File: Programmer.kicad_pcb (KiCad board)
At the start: 2 copper layers, 17.8 x 38.1 mm, 10 parts, among them J1 USB_B_Micro, J2 Conn_02x05_Odd_Even, SW1 SW_Push, U1 MKL04Z32VLC4, U2 ADP2108AUJ-3.3

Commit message: Rounded corners, added LED
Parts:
- added D1: LED, LED_SMD:LED_0805_2012Metric_Pad1.15x1.40mm_HandSolder, F.Cu at (139.1, 108.6)
- added R3: 500, Resistor_SMD:R_0805_2012Metric_Pad1.15x1.40mm_HandSolder, F.Cu at (139.1, 106.4)
- moved U2 2.16 mm to (135.0, 108.0)
- moved SW1 0.25 mm to (147.2, 101.0)
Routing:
- net +3V3: track 30.1 -> 33.6 mm
- net Net-(D1-Pad1): track 0.00 -> 3.01 mm
- net GND: track 23.7 -> 25.9 mm, vias 6 -> 7
- net Net-(L1-Pad1): track 3.85 -> 2.62 mm
- net /PTA1: track 33.8 -> 34.3 mm
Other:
- outline, holes or cut-outs redrawn

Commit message: Added silkscreen
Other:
- board text added: "RMTS Programmer Rev 1 Andrew Reilley, 2021"
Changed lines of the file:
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@@
   (general
     (thickness 1.6)
-    (drawings 8)
+    (drawings 9)
     (tracks 155)
     (zones 0)
@@
     )
   )
+  (gr_text "RMTS Programmer Rev 1\nAndrew Reilley, 2021" (at 135.89 101.346 90) (layer B.SilkS)
+    (effects (font (size 1.5 1.5) (thickness 0.3)) (justify mirror))
+  )
   (gr_line (start 131.445 117.094) (end 131.445 83.312) (layer Edge.Cuts) (width 0.1))

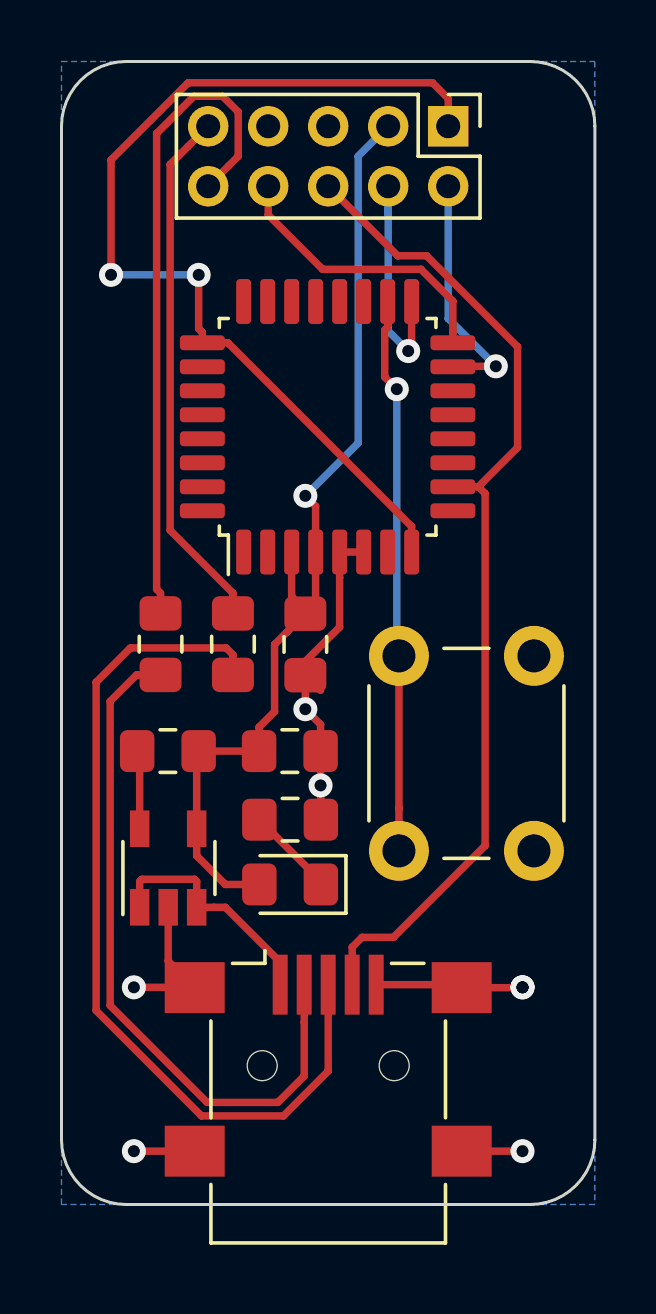
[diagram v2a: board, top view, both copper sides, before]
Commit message: Add input cap
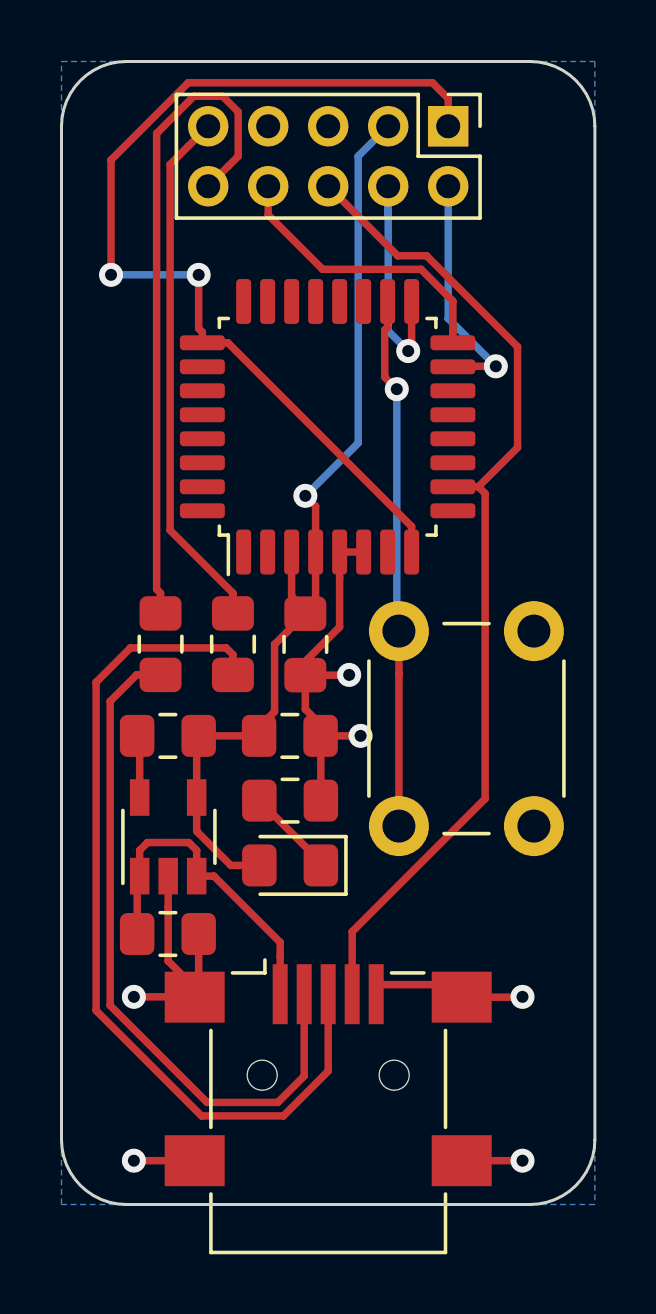
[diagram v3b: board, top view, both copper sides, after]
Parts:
- added C3: 4.7uF, Capacitor_SMD:C_0805_2012Metric_Pad1.15x1.40mm_HandSolder, F.Cu at (135.0, 110.2)
- R1, R2: value R_US -> 33
- moved U2 1.04 mm to (135.0, 107.0)
- moved SW1 0.83 mm to (147.2, 100.1)
- moved R3 0.64 mm to (139.1, 105.8)
- moved D1 0.63 mm to (139.1, 108.0)
- moved C2 0.51 mm to (139.1, 103.6)
- moved L1 0.51 mm to (135.0, 103.6)
- moved J1 0.32 mm to (140.3, 114.9)
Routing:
- net GND: track 25.9 -> 30.2 mm, vias 7 -> 6
- net Net-(C3-Pad1): track 7.97 -> 11.2 mm
- net +3V3: track 33.6 -> 32.8 mm
- net Net-(SW1-Pad2): track 18.8 -> 19.5 mm
- net Net-(L1-Pad1): track 2.62 -> 2.09 mm

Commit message: Provide 5v to target
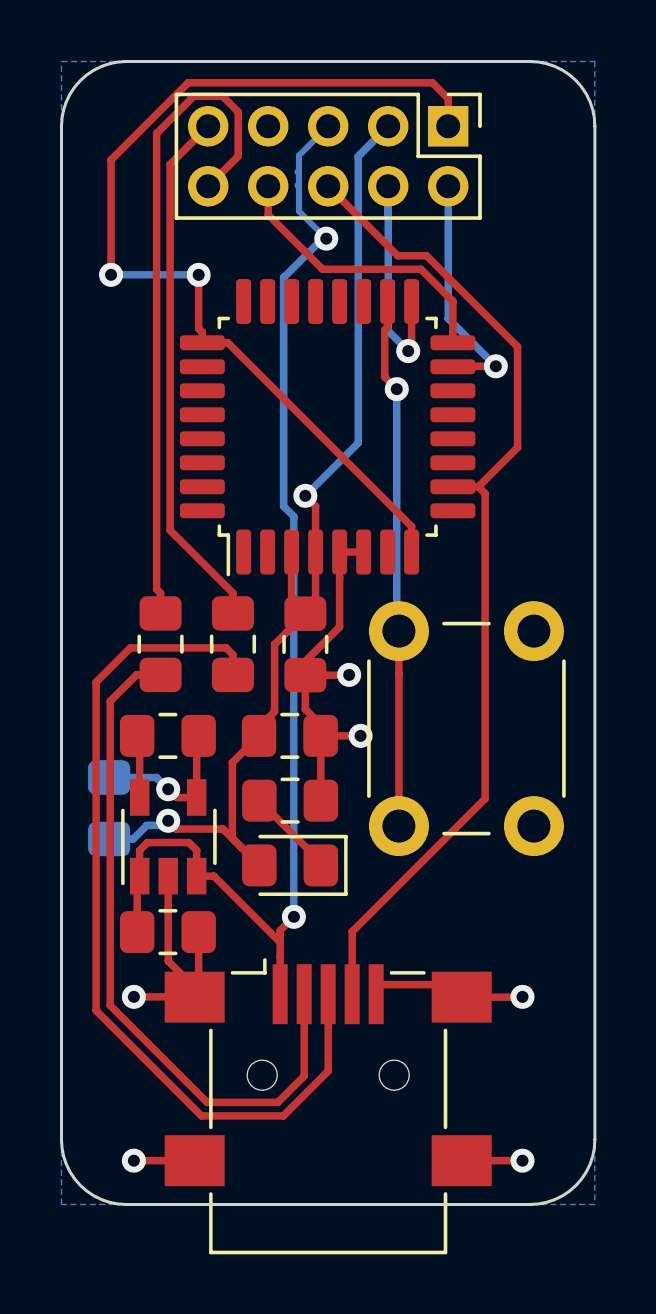
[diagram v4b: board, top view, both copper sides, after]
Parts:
- added 3v3: 0, Resistor_SMD:R_0805_2012Metric_Pad1.15x1.40mm_HandSolder, B.Cu at (133.0, 106.0)
- moved C3 0.06 mm to (135.0, 110.2)
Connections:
- C3 pad 1: Net-(C3-Pad1) -> +5V
- J1 pad 1: Net-(C3-Pad1) -> +5V
- J2 pad 5: GND -> +5V
- L1 pad 2: +3V3 -> Net-(L1-Pad2)
- U2 pad 1: Net-(C3-Pad1) -> +5V
- U2 pad 3: Net-(C3-Pad1) -> +5V
- U2 pad 4: +3V3 -> Net-(L1-Pad2)
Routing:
- net +5V: track 0.00 -> 40.2 mm, vias 0 -> 2
- net Net-(C3-Pad1): track 11.2 -> 0.00 mm
- net Net-(L1-Pad2): track 0.00 -> 5.85 mm, vias 0 -> 1
- net +3V3: track 32.8 -> 34.6 mm, vias 1 -> 2
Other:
- net class Small added: clearance 0.2, trace_width 0.2, via_dia 0.8, via_drill 0.4

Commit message: Add 0 ohm resistor to ID pin, cleanup
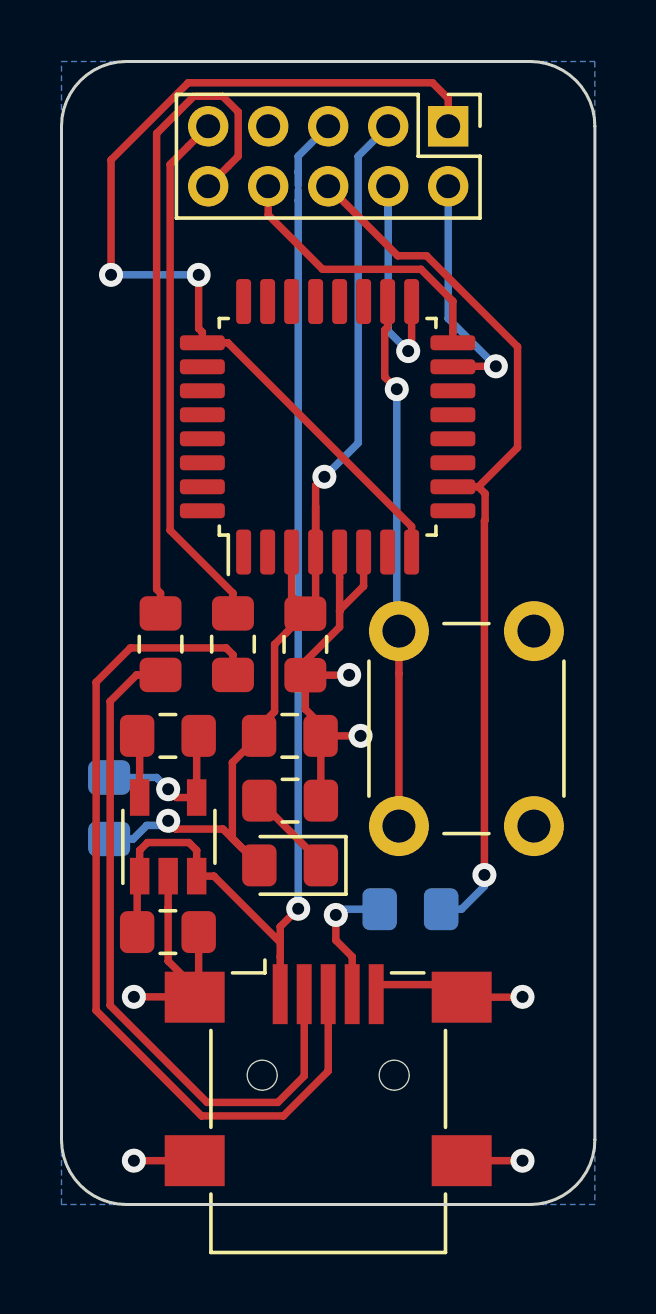
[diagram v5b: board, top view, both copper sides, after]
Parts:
- added ID: 0, Resistor_SMD:R_0805_2012Metric_Pad1.15x1.40mm_HandSolder, B.Cu at (143.1, 109.4)
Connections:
- J1 pad 4: /PTA1 -> Net-(J1-Pad4)
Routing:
- net Net-(J1-Pad4): track 0.00 -> 4.41 mm, vias 0 -> 1
- net /PTA1: track 34.0 -> 30.4 mm, vias 0 -> 1
- net GND: track 30.2 -> 31.7 mm
- net +3V3: track 34.6 -> 35.9 mm
- net +5V: track 40.2 -> 39.1 mm, vias 2 -> 1
